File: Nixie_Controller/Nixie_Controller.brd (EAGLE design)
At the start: 150 x 100 mm, 69 parts, among them IC1 4028N, T1 MMBTA42, T10 MMBTA42, T11 MMBTA42, T12 MMBTA42, T13 MMBTA42, T14 MMBTA42, T15 MMBTA42, T16 MMBTA42, T17 MMBTA42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

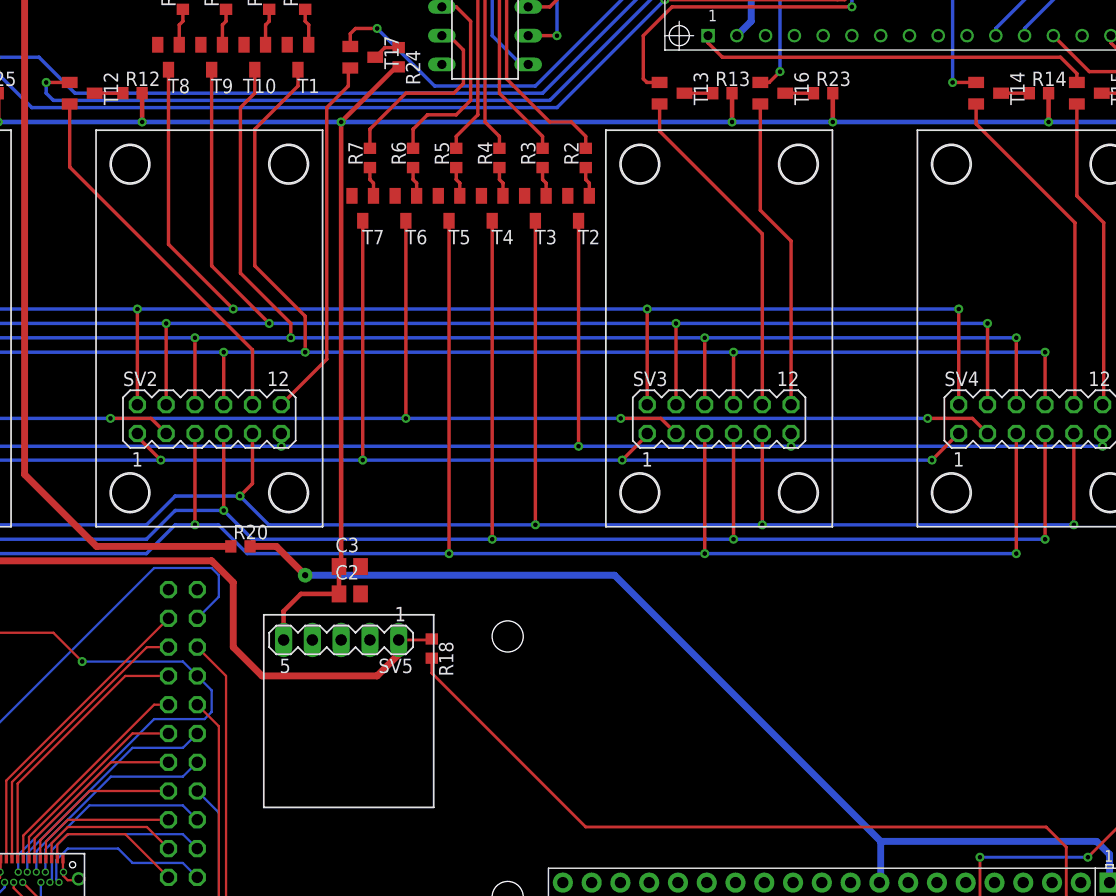
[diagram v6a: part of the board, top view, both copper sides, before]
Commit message: fix: Reroute
Reroute multiple connections for cleaner looks.
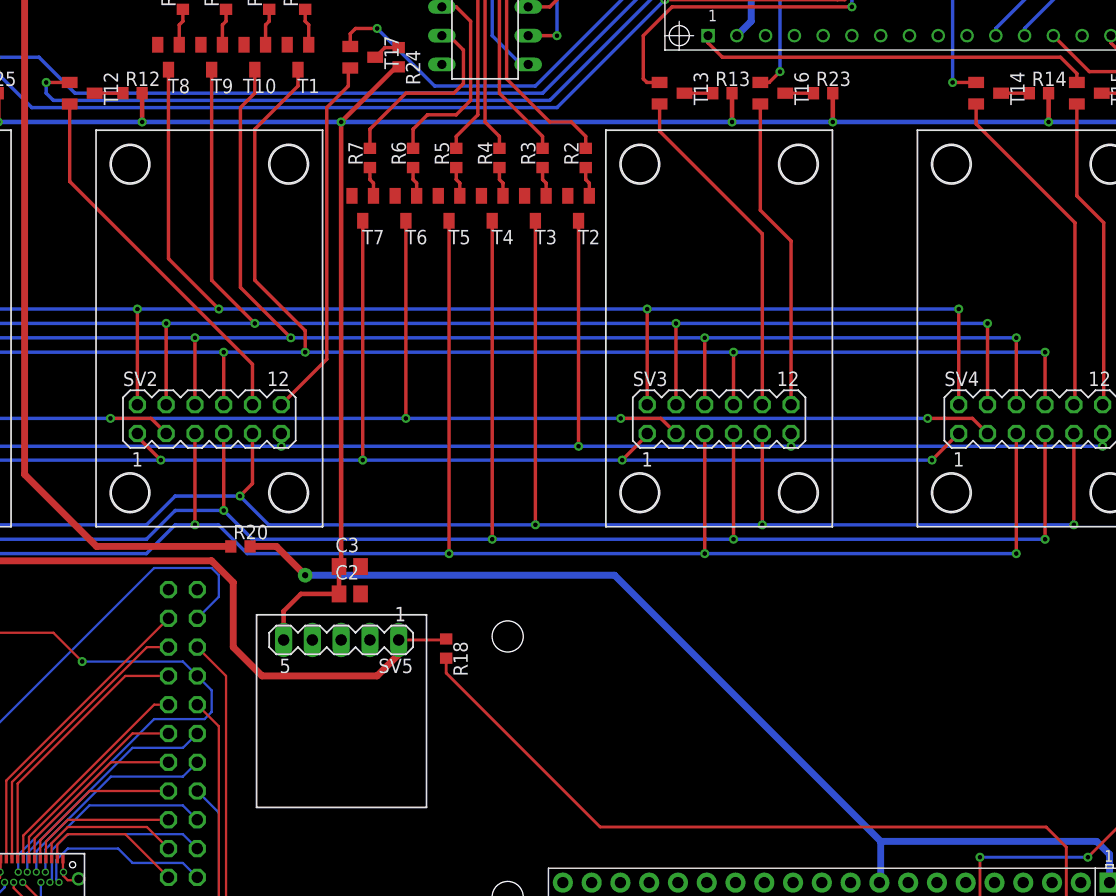
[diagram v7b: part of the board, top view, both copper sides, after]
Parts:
- moved R18 1.27 mm to (73.4, 26.5)
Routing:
- net VDD: track 309.7 -> 311.0 mm
- net +5V: track 72.4 -> 71.2 mm
- net N$28: track 153.4 -> 152.8 mm
- net N$27: track 157.3 -> 156.7 mm
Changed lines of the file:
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@@
 <wire x1="150" y1="100" x2="0" y2="100" width="0" layer="20"/>
 <wire x1="0" y1="100" x2="0" y2="0" width="0" layer="20"/>
-<wire x1="72.305" y1="29.525" x2="72.305" y2="12.525" width="0.1524" layer="21"/>
-<wire x1="72.305" y1="12.525" x2="57.305" y2="12.525" width="0.1524" layer="21"/>
-<wire x1="57.305" y1="12.525" x2="57.305" y2="29.525" width="0.1524" layer="21"/>
-<wire x1="57.305" y1="29.525" x2="72.305" y2="29.525" width="0.1524" layer="21"/>
+<wire x1="71.67" y1="29.525" x2="71.67" y2="12.525" width="0.1524" layer="21"/>
+<wire x1="71.67" y1="12.525" x2="56.67" y2="12.525" width="0.1524" layer="21"/>
+<wire x1="56.67" y1="12.525" x2="56.67" y2="29.525" width="0.1524" layer="21"/>
+<wire x1="56.67" y1="29.525" x2="71.67" y2="29.525" width="0.1524" layer="21"/>
 <wire x1="15" y1="72.3" x2="15" y2="37.3" width="0.1524" layer="21"/>
 <wire x1="15" y1="37.3" x2="35" y2="37.3" width="0.1524" layer="21"/>
@@
 <element name="R17" library="resistor" package="R0603" value="10k" x="142.875" y="73.025" rot="R180"/>
 <element name="R19" library="resistor" package="R0603" value="0" x="142.875" y="75.565" rot="R180"/>
-<element name="R18" library="resistor" package="R0603" value="0" x="72.136" y="26.543" rot="R270"/>
+<element name="R18" library="resistor" package="R0603" value="0" x="73.406" y="26.543" rot="R270"/>
 <element name="R20" library="resistor" package="R0603" value="0" x="55.245" y="35.56"/>
 <element name="R21" library="resistor" package="R0603" value="0" x="46.99" y="92.71"/>
@@
 <wire x1="141.224" y1="98.171" x2="143.725" y2="95.67" width="0.6096" layer="1"/>
 <wire x1="143.725" y1="95.67" x2="143.725" y2="75.565" width="0.6096" layer="1"/>
-<wire x1="69.215" y1="27.305" x2="72.048" y2="27.305" width="0.254" layer="1"/>
-<wire x1="72.048" y1="27.305" x2="72.136" y2="27.393" width="0.254" layer="1"/>
+<wire x1="69.215" y1="27.305" x2="73.318" y2="27.305" width="0.254" layer="1"/>
+<wire x1="73.318" y1="27.305" x2="73.406" y2="27.393" width="0.254" layer="1"/>
 </signal>
 <signal name="N$1">
@@
 <via x="18.65" y="56.515" extent="1-16" drill="0.4" diameter="0.65"/>
 <wire x1="18.65" y1="56.515" x2="18.65" y2="48.07" width="0.3048" layer="1"/>
-<wire x1="46.15" y1="56.515" x2="54.61" y2="56.515" width="0.3048" layer="16"/>
-<wire x1="54.61" y1="56.515" x2="91.15" y2="56.515" width="0.3048" layer="16"/>
+<wire x1="46.15" y1="56.515" x2="53.34" y2="56.515" width="0.3048" layer="16"/>
+<wire x1="53.34" y1="56.515" x2="91.15" y2="56.515" width="0.3048" layer="16"/>
 <wire x1="91.15" y1="56.515" x2="118.65" y2="56.515" width="0.3048" layer="16"/>
 <wire x1="91.15" y1="48.07" x2="91.15" y2="56.515" width="0.3048" layer="1"/>
@@
 <via x="118.65" y="56.515" extent="1-16" drill="0.4" diameter="0.65"/>
 <via x="91.15" y="56.515" extent="1-16" drill="0.4" diameter="0.65"/>
-<wire x1="48.895" y1="77.64" x2="48.895" y2="62.23" width="0.3048" layer="1"/>
-<wire x1="48.895" y1="62.23" x2="54.61" y2="56.515" width="0.3048" layer="1"/>
-<via x="54.61" y="56.515" extent="1-16" drill="0.4" diameter="0.65"/>
+<wire x1="48.895" y1="77.64" x2="48.895" y2="60.96" width="0.3048" layer="1"/>
+<wire x1="48.895" y1="60.96" x2="53.34" y2="56.515" width="0.3048" layer="1"/>
+<via x="53.34" y="56.515" extent="1-16" drill="0.4" diameter="0.65"/>
 </signal>
 <signal name="N$28">
@@
 <via x="21.19" y="55.245" extent="1-16" drill="0.4" diameter="0.65"/>
 <wire x1="21.19" y1="55.245" x2="21.19" y2="48.07" width="0.3048" layer="1"/>
-<wire x1="48.69" y1="55.245" x2="57.785" y2="55.245" width="0.3048" layer="16"/>
-<wire x1="57.785" y1="55.245" x2="93.69" y2="55.245" width="0.3048" layer="16"/>
+<wire x1="48.69" y1="55.245" x2="56.515" y2="55.245" width="0.3048" layer="16"/>
+<wire x1="56.515" y1="55.245" x2="93.69" y2="55.245" width="0.3048" layer="16"/>
 <wire x1="93.69" y1="55.245" x2="121.19" y2="55.245" width="0.3048" layer="16"/>
 <wire x1="93.69" y1="48.07" x2="93.69" y2="55.245" width="0.3048" layer="1"/>
@@
 <via x="121.19" y="55.245" extent="1-16" drill="0.4" diameter="0.65"/>
 <via x="93.69" y="55.245" extent="1-16" drill="0.4" diameter="0.65"/>
-<wire x1="52.705" y1="77.64" x2="52.705" y2="60.325" width="0.3048" layer="1"/>
-<wire x1="52.705" y1="60.325" x2="57.785" y2="55.245" width="0.3048" layer="1"/>
-<via x="57.785" y="55.245" extent="1-16" drill="0.4" diameter="0.65"/>
+<wire x1="52.705" y1="77.64" x2="52.705" y2="59.055" width="0.3048" layer="1"/>
+<wire x1="52.705" y1="59.055" x2="56.515" y2="55.245" width="0.3048" layer="1"/>
+<via x="56.515" y="55.245" extent="1-16" drill="0.4" diameter="0.65"/>
 </signal>
 <signal name="N$29">
@@
 <wire x1="56.515" y1="77.64" x2="56.515" y2="75.565" width="0.3048" layer="1"/>
 <wire x1="56.515" y1="75.565" x2="55.245" y2="74.295" width="0.3048" layer="1"/>
-<wire x1="55.245" y1="74.295" x2="55.245" y2="59.69" width="0.3048" layer="1"/>
-<wire x1="55.245" y1="59.69" x2="59.69" y2="55.245" width="0.3048" layer="1"/>
-<wire x1="59.69" y1="55.245" x2="59.69" y2="53.975" width="0.3048" layer="1"/>
+<wire x1="55.245" y1="74.295" x2="55.245" y2="58.42" width="0.3048" layer="1"/>
+<wire x1="55.245" y1="58.42" x2="59.69" y2="53.975" width="0.3048" layer="1"/>
 <via x="59.69" y="53.975" extent="1-16" drill="0.4" diameter="0.65"/>
 </signal>
@@
 <via x="98.77" y="52.705" extent="1-16" drill="0.4" diameter="0.65"/>
 <wire x1="60.325" y1="77.64" x2="60.325" y2="76.2" width="0.3048" layer="1"/>
-<wire x1="56.515" y1="60.325" x2="60.96" y2="55.88" width="0.3048" layer="1"/>
-<wire x1="60.96" y1="55.88" x2="60.96" y2="52.705" width="0.3048" layer="1"/>
+<wire x1="56.515" y1="59.055" x2="60.96" y2="54.61" width="0.3048" layer="1"/>
+<wire x1="60.96" y1="54.61" x2="60.96" y2="52.705" width="0.3048" layer="1"/>
 <via x="60.96" y="52.705" extent="1-16" drill="0.4" diameter="0.65"/>
 <wire x1="60.325" y1="76.2" x2="56.515" y2="72.39" width="0.3048" layer="1"/>
-<wire x1="56.515" y1="72.39" x2="56.515" y2="60.325" width="0.3048" layer="1"/>
+<wire x1="56.515" y1="72.39" x2="56.515" y2="59.055" width="0.3048" layer="1"/>
 </signal>
 <signal name="+170V">
@@
 <contactref element="SV2" pad="10"/>
 <contactref element="T12" pad="2"/>
-<wire x1="56.31" y1="52.91" x2="56.31" y2="48.07" width="0.3048" layer="1"/>
-<wire x1="40.175" y1="74.615" x2="40.175" y2="69.045" width="0.3048" layer="1"/>
-<wire x1="40.175" y1="69.045" x2="56.31" y2="52.91" width="0.3048" layer="1"/>
+<wire x1="56.31" y1="51.64" x2="56.31" y2="48.07" width="0.3048" layer="1"/>
+<wire x1="40.175" y1="74.615" x2="40.175" y2="67.775" width="0.3048" layer="1"/>
+<wire x1="40.175" y1="67.775" x2="56.31" y2="51.64" width="0.3048" layer="1"/>
 </signal>
 <signal name="N$38">
@@
 <contactref element="R18" pad="2"/>
 <wire x1="129.425" y1="3.345" x2="131.965" y2="3.345" width="0.254" layer="1"/>
-<wire x1="85.725" y1="10.795" x2="126.365" y2="10.795" width="0.254" layer="1"/>
+<wire x1="86.995" y1="10.795" x2="126.365" y2="10.795" width="0.254" layer="1"/>
 <wire x1="126.365" y1="10.795" x2="128.143" y2="9.017" width="0.254" layer="1"/>
 <wire x1="128.143" y1="4.627" x2="129.425" y2="3.345" width="0.254" layer="1"/>
 <wire x1="128.143" y1="9.017" x2="128.143" y2="4.627" width="0.254" layer="1"/>
-<wire x1="72.136" y1="25.693" x2="72.136" y2="24.384" width="0.254" layer="1"/>
-<wire x1="72.136" y1="24.384" x2="85.725" y2="10.795" width="0.254" layer="1"/>
+<wire x1="73.406" y1="25.693" x2="73.406" y2="24.384" width="0.254" layer="1"/>
+<wire x1="73.406" y1="24.384" x2="86.995" y2="10.795" width="0.254" layer="1"/>
 </signal>
 <signal name="N$57">

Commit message: fix: Change names
Change the names of the Raspberry Pi and the USB-C connectors to something more meaningfull.
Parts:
- renumbered U$1 to RPI, U$2 to USBC2, U$3 to USBC1
